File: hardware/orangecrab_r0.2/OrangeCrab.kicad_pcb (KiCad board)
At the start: 6 copper layers, 50.8 x 22.9 mm, 160 parts, among them J1 Conn_01x12_Male, J2 Conn_01x16_Male, J3 USB_B_Micro, J4 MicroSd, J5 JST, J6 JTAG, SW1 SW_Push, U1 FAN53541, U10 NCP115-2.5, U2 FAN53541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

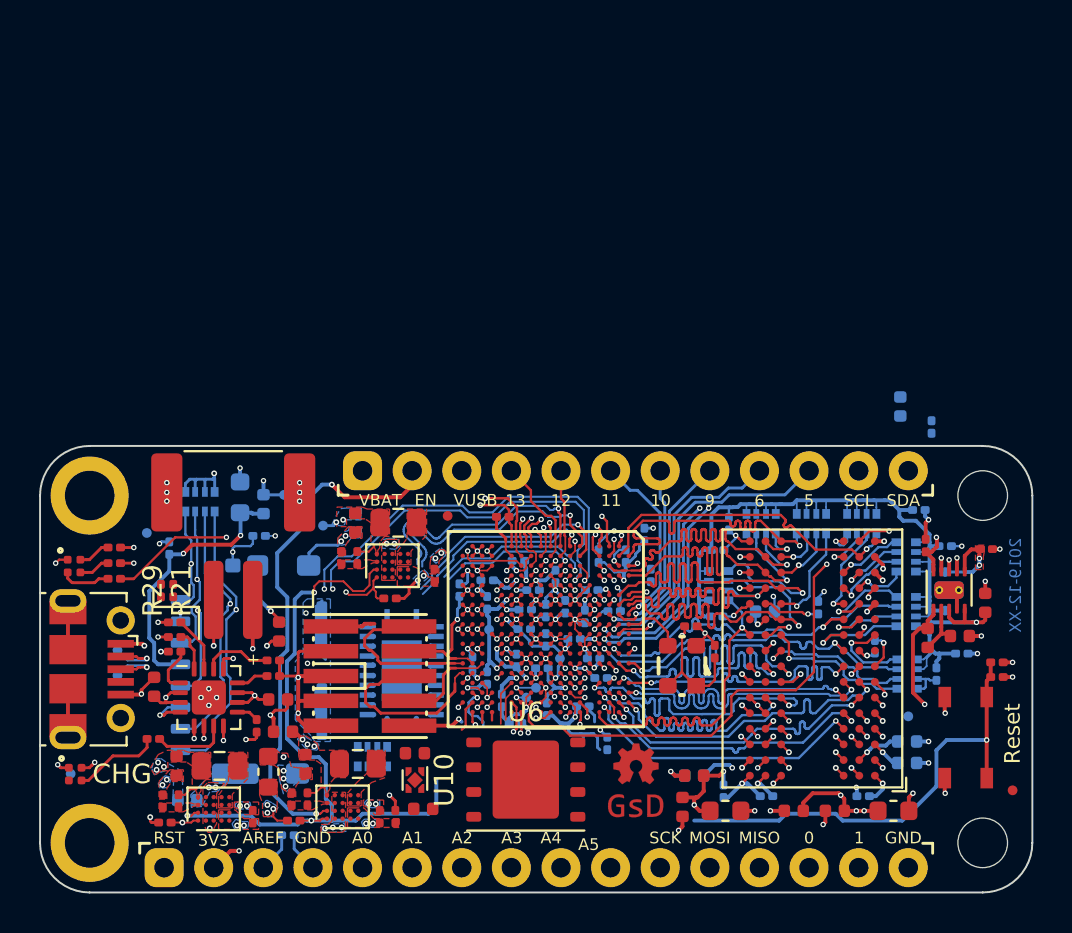
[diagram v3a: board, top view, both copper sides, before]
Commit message: hw: Update microSD card
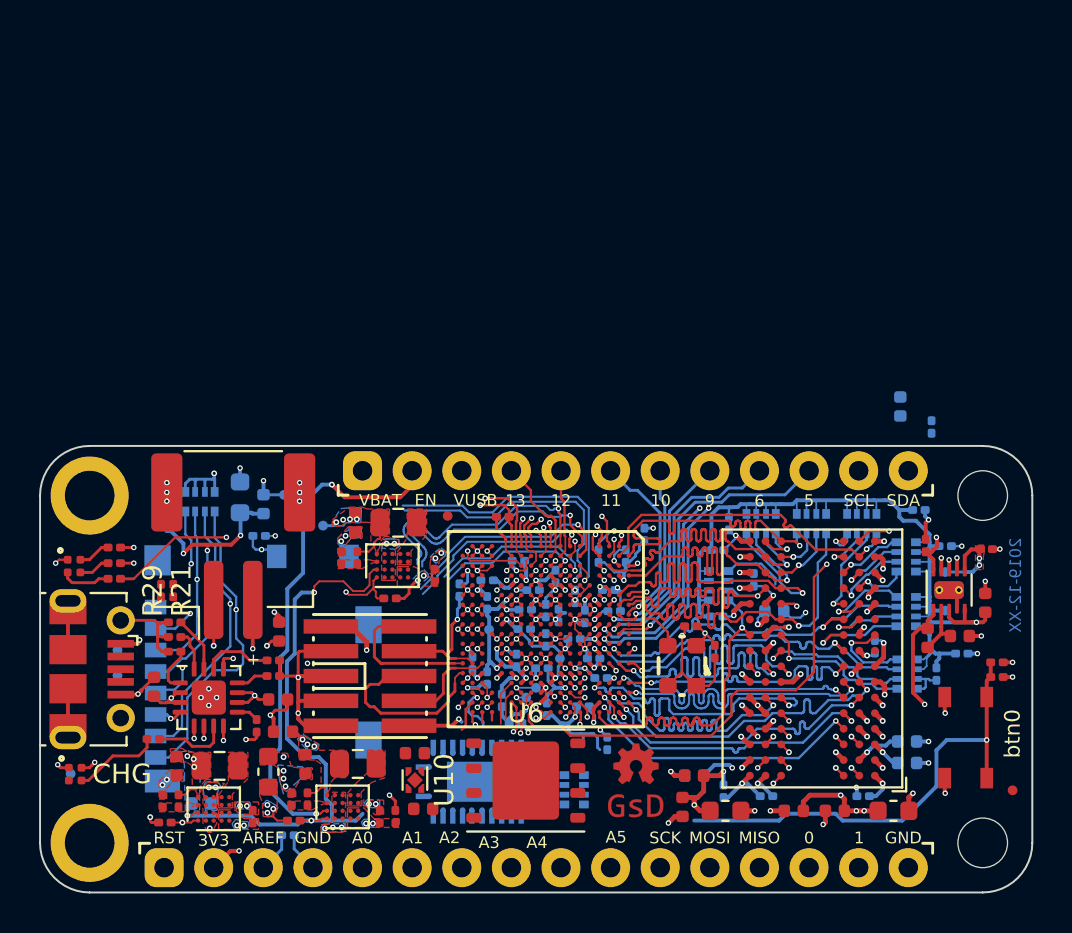
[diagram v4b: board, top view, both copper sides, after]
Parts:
- removed the REF** at (179.0, 105.4)
- removed the REF** at (140.0, 96.0)
- J4: footprint gkl_conn:micro_sd_1051620001 -> gkl_conn:molex_microsd_1040310811
- moved RN9 10.5 mm to (161.9, 109.1), turned to 180 degrees
- moved U9 6.87 mm to (156.9, 108.7), turned to 90 degrees
- moved J4 5.35 mm to (140.4, 102.9)
- moved C62 4.02 mm to (161.9, 99.2)
- moved C44 3.59 mm to (171.1, 98.4)
- moved C70 1.33 mm to (141.1, 95.4)
- moved C68 0.88 mm to (163.6, 98.9), turned to 0 degrees
- moved C7 0.75 mm to (142.8, 109.8)
- moved C48 0.57 mm to (161.1, 100.2)
- moved R19 0.48 mm to (172.1, 100.0)
- moved U6 0.05 mm to (159.4, 108.7)
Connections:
- RN1 pad 8: Net-(RN1-Pad8) -> RAM_A12
- RN4 pad 5: RAM_A12 -> RAM_A15
- RN4 pad 6: RAM_A10 -> Net-(RN4-Pad6)
- RN8 pad 5: RAM_A15 -> RAM_A10
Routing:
- net ADC_CTRL1: track 30.0 -> 15.0 mm, vias 2 -> 1
- net ADC_CTRL0: track 28.3 -> 14.1 mm, vias 2 -> 1
- net P3.3V: track 45.0 -> 57.8 mm, vias 19 -> 20
- net Net-(U3-PadN4): track 13.4 -> 4.60 mm
- net USB_D+: track 30.9 -> 22.5 mm, vias 2 -> 1
- net Net-(U3-PadN3): track 13.1 -> 4.71 mm
- net USB_D-: track 32.1 -> 24.0 mm, vias 2 -> 1
- net GND: track 183.9 -> 177.7 mm, vias 137 -> 130
- net /sheetPower/PGOOD_P1.1V: track 35.3 -> 30.0 mm
- net ADC_MUX1: track 15.2 -> 10.2 mm
- net ADC_MUX0: track 14.3 -> 10.3 mm
- net SD0_DAT2: track 27.3 -> 24.5 mm
- net ADC_SENSE_LO: track 11.9 -> 9.13 mm
- net Net-(C70-Pad2): track 13.5 -> 15.4 mm, vias 2 -> 3
- net SD0_CD: track 21.2 -> 19.4 mm
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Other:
- net class DDR3_CTRL_LM1.0: clearance 0.1778 -> 0.1016
- board text added: "btn0"
- board text removed: "Reset"

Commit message: hw: Routed new FLASH footprint Working on new Analog domain
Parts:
- moved C69 2.24 mm to (161.0, 106.4), turned to 90 degrees
- moved U10 0.11 mm to (153.6, 108.7)
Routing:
- net SPI_CONFIG_MOSI: track 0.71 -> 10.6 mm, vias 1 -> 2
- net GND: track 177.7 -> 186.5 mm, vias 130 -> 135
- net SPI_CONFIG_SCK: track 2.56 -> 11.3 mm, vias 1 -> 2
- net QSPI_D3: track 0.40 -> 8.81 mm, vias 0 -> 2
- net /sheetIO/A5: track 0.00 -> 6.51 mm
- net /sheetIO/A0: track 0.00 -> 6.48 mm
- net P3.3V: track 57.8 -> 63.0 mm, vias 20 -> 22
- net /sheetIO/A4: track 0.00 -> 4.58 mm
- net /sheetIO/A1: track 0.00 -> 4.44 mm
- net QSPI_D2: track 0.42 -> 4.81 mm
- net IO_MOSI: track 13.7 -> 17.9 mm, vias 0 -> 1
- net VTT_REF: track 32.6 -> 36.3 mm
- net /sheetPower/PGOOD_P1.1V: track 30.0 -> 33.1 mm, vias 3 -> 4
- net /sheetIO/A2: track 0.00 -> 3.04 mm
- net /sheetIO/A3: track 0.00 -> 3.02 mm
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
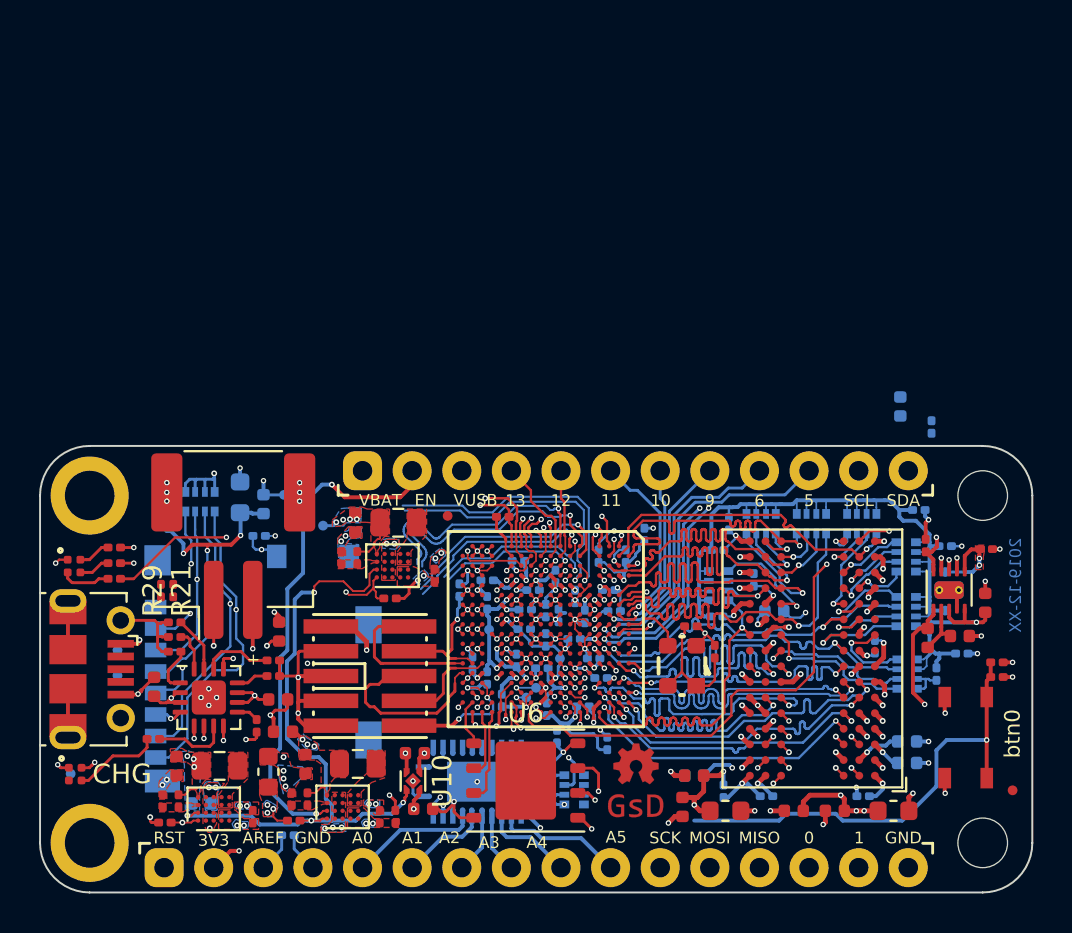
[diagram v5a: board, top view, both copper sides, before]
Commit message: hw: Routed analog section General cleanup
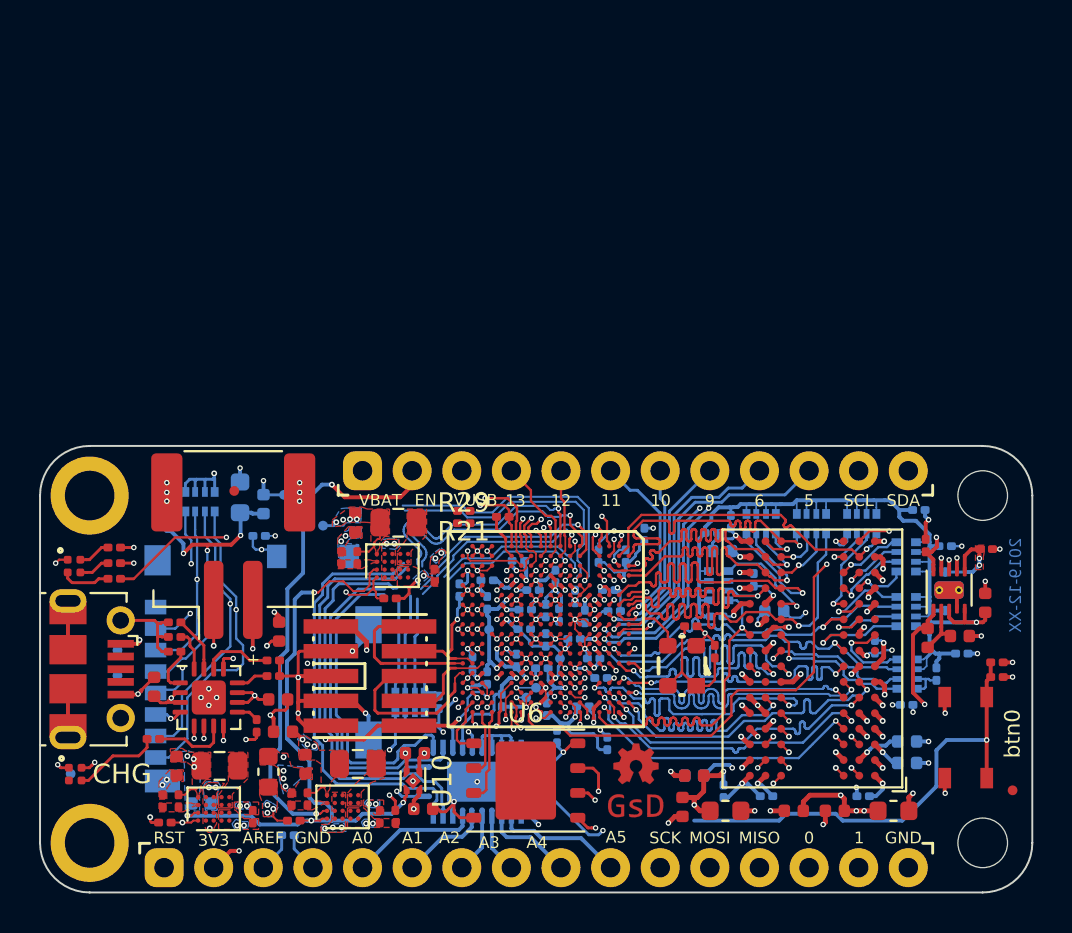
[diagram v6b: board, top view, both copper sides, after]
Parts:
- added C28: C, Capacitor_SMD:C_0201_0603Metric, B.Cu at (154.9, 104.7)
- moved R21 16.0 mm to (156.2, 94.8), turned to 180 degrees
- moved R29 15.3 mm to (156.2, 95.5), turned to 0 degrees
- moved C32 14.3 mm to (178.9, 104.8), turned to 0 degrees
- moved C36 11.7 mm to (169.4, 96.9), turned to 180 degrees
- moved REF** 11.0 mm to (144.5, 93.8)
- moved RN9 9.52 mm to (153.5, 104.7), turned to 270 degrees
- moved C42 0.93 mm to (168.9, 96.0)
- moved C40 0.14 mm to (169.9, 95.4)
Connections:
- U9 pad 16: Net-(U9-Pad16) -> P1.1V
- U9 pad 17: Net-(U9-Pad17) -> P1.35V
- U9 pad 18: Net-(U9-Pad18) -> P2.5V
- U9 pad 19: Net-(U9-Pad19) -> GND
- U9 pad 2: P3.3V -> /sheetIO/AREF
- U9 pad 20: Net-(U9-Pad20) -> GND
- U9 pad 21: P1.2V -> GND
- U9 pad 22: P1.35V -> GND
- U9 pad 23: P2.5V -> P3.3V
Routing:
- net ADC_MUX0: track 10.9 -> 32.3 mm, vias 2 -> 1
- net ADC_MUX1: track 11.4 -> 32.4 mm, vias 2 -> 1
- net ADC_MUX3: track 8.45 -> 26.1 mm
- net ADC_CTRL1: track 15.0 -> 32.2 mm
- net Net-(RN9-Pad8): track 2.36 -> 19.4 mm, vias 0 -> 2
- net ADC_MUX2: track 7.08 -> 23.3 mm
- net GND: track 186.5 -> 202.5 mm, vias 135 -> 140
- net ADC_CTRL0: track 15.5 -> 22.5 mm, vias 2 -> 1
- net ADC_SENSE_LO: track 9.13 -> 15.8 mm
- net ADC_SENSE_HI: track 10.1 -> 16.2 mm
- net P1.1V: track 46.5 -> 51.4 mm, vias 13 -> 14
- net P1.35V: track 84.7 -> 88.9 mm
- net FPGA_RESET: track 25.2 -> 23.5 mm, vias 2 -> 3
- net /sheetIO/AREF: track 2.05 -> 3.10 mm, vias 0 -> 1
- net /sheetHyperRAM/RAM_VDD: track 17.0 -> 17.9 mm, vias 11 -> 12
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
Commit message: hw: Update board with 3d models Finish pin-swaps and routing of open changes General cleanups
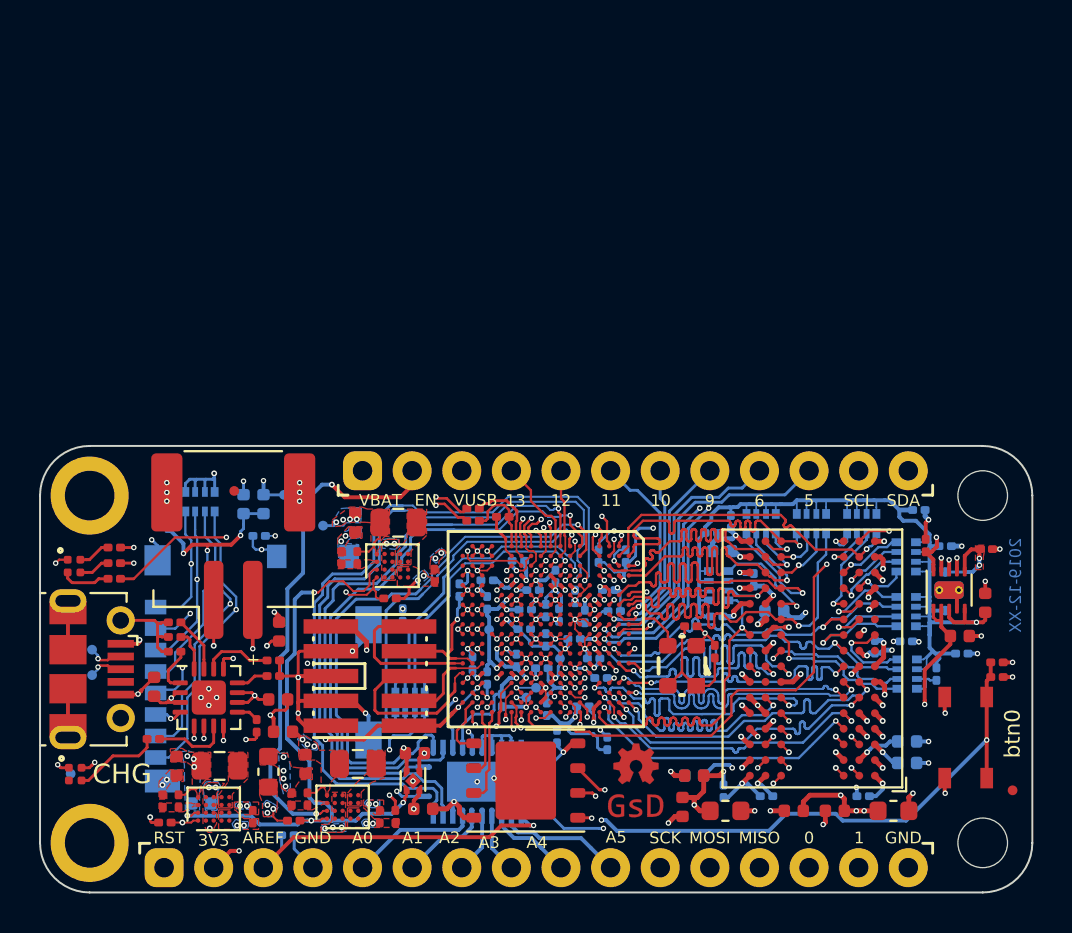
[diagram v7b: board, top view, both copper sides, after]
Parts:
- removed C71: 4.7uF, Capacitor_SMD:C_0603_1608Metric
- removed R3: 0R, Resistor_SMD:R_0201_0603Metric
- removed R6: 0R, Resistor_SMD:R_0402_1005Metric
- added C29: 10uF, Capacitor_SMD:C_0402_1005Metric, B.Cu at (144.9, 94.5)
- moved C28 4.84 mm to (153.1, 100.2), turned to 90 degrees
- moved C32 3.25 mm to (178.9, 101.5)
- moved TP26 1.30 mm to (137.2, 103.3)
- moved TP27 1.30 mm to (137.2, 102.0)
- moved R29 0.89 mm to (156.7, 94.7), turned to 180 degrees
- moved R21 0.69 mm to (156.7, 95.3), turned to 0 degrees
- turned RN9 to 90 degrees
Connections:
- C10 pad 2: VTT_REF -> ECP5_VREF
- C44 pad 2: VTT_REF -> ECP5_VREF
- C45 pad 2: VTT_REF -> ECP5_VREF
- C8 pad 2: Net-(C8-Pad2) -> P1.35V
- J3 pad 2: Net-(J3-Pad2) -> /sheetIO/_USB_D_N
- J3 pad 3: Net-(J3-Pad3) -> /sheetIO/_USB_D_P
- R20 pad 1: Net-(J3-Pad3) -> USB_D+
- R21 pad 1: Net-(J3-Pad3) -> /sheetIO/_USB_D_P
- R29 pad 2: Net-(J3-Pad2) -> /sheetIO/_USB_D_N
- RN9 pad 1: ADC_SENSE_HI -> Net-(RN9-Pad1)
- RN9 pad 2: ADC_SENSE_HI -> GND
- RN9 pad 3: ADC_SENSE_LO -> ADC_CTRL0
- RN9 pad 4: ADC_SENSE_LO -> ADC_CTRL0
- RN9 pad 5: ADC_CTRL0 -> ADC_SENSE_LO
- RN9 pad 6: ADC_CTRL0 -> ADC_SENSE_LO
- RN9 pad 7: GND -> ADC_SENSE_HI
- RN9 pad 8: Net-(RN9-Pad8) -> ADC_SENSE_HI
- TP26 pad 1: USB_D+ -> /sheetIO/_USB_D_P
- TP27 pad 1: USB_D- -> /sheetIO/_USB_D_N
- TP28 pad 1: VTT_REF -> ECP5_VREF
- U3 pad F1: Net-(U3-PadF1) -> ADC_CTRL1
- U3 pad F2: Net-(U3-PadF2) -> ADC_MUX2
- U3 pad F3: ADC_CTRL1 -> ADC_MUX1
- U3 pad F4: ADC_CTRL0 -> ADC_MUX0
- U3 pad G1: Net-(U3-PadG1) -> ADC_CTRL0
- U3 pad G3: ADC_MUX3 -> ADC_SENSE_LO
- U3 pad G4: ADC_MUX1 -> Net-(U3-PadG4)
- U3 pad H1: Net-(U3-PadH1) -> ADC_MUX3
- U3 pad H3: ADC_MUX2 -> ADC_SENSE_HI
- U3 pad H4: ADC_MUX0 -> Net-(U3-PadH4)
- U3 pad K4: ADC_SENSE_HI -> LED_R
- U3 pad L4: ADC_SENSE_LO -> Net-(U3-PadL4)
- U3 pad M3: Net-(U3-PadM3) -> LED_G
- U3 pad R16: FPGA_RESET -> Net-(U3-PadR16)
- U3 pad T17: LED_G -> USER_BUTTON
- U3 pad V17: LED_R -> FPGA_RESET
- U4 pad H1: VTT_REF -> ECP5_VREF
- U4 pad M8: VTT_REF -> ECP5_VREF
- U8 pad 2: Net-(C8-Pad2) -> P1.35V
- U8 pad 6: VTT_REF -> ECP5_VREF
- U9 pad 1: Net-(RN9-Pad8) -> Net-(RN9-Pad1)
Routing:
- net ECP5_VREF: track 20.3 -> 60.8 mm, vias 4 -> 9
- net VTT_REF: track 36.3 -> 0.00 mm, vias 5 -> 0
- net /sheetIO/_USB_D_N: track 0.00 -> 27.5 mm, vias 0 -> 2
- net /sheetIO/_USB_D_P: track 0.00 -> 27.5 mm, vias 0 -> 2
- net Net-(RN9-Pad1): track 0.00 -> 21.8 mm, vias 0 -> 2
- net Net-(RN9-Pad8): track 19.4 -> 0.00 mm, vias 2 -> 0
- net USB_D-: track 24.0 -> 4.75 mm, vias 1 -> 0
- net USB_D+: track 22.5 -> 4.08 mm, vias 1 -> 0
- net USER_BUTTON: track 24.1 -> 39.5 mm, vias 1 -> 3
- net Net-(U3-PadM3): track 14.5 -> 0.00 mm, vias 1 -> 0
- net /sheetIO/AREF: track 3.10 -> 17.6 mm
- net Net-(U3-PadF1): track 13.7 -> 0.00 mm, vias 1 -> 0
- net Net-(U3-PadH1): track 13.5 -> 0.00 mm, vias 1 -> 0
- net Net-(U3-PadF2): track 11.6 -> 0.00 mm, vias 1 -> 0
- net LED_R: track 25.3 -> 36.5 mm
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- added copper zone on F.Cu, net ECP5_VREF
- removed copper zone on F.Cu, net VTT_REF
- removed copper zone on In3.Cu, net VTT_REF
